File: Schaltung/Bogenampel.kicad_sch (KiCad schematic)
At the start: 36 parts, among them J1 WS2812B Stripe Timer, J10 Display, J2 Conn_01x04_Pin, J3 DC/DC Boost, J4 Jumper: 5V/Ext Voltage, J5 Buzzer, J6 Battery, J7 Input 4, J8 Input 5, J9 Power Bank, Q1 IRLZ44N, U1 NRF24L01_Breakout, U2 TXS0108EPW, U3 LM1117DT-3.3

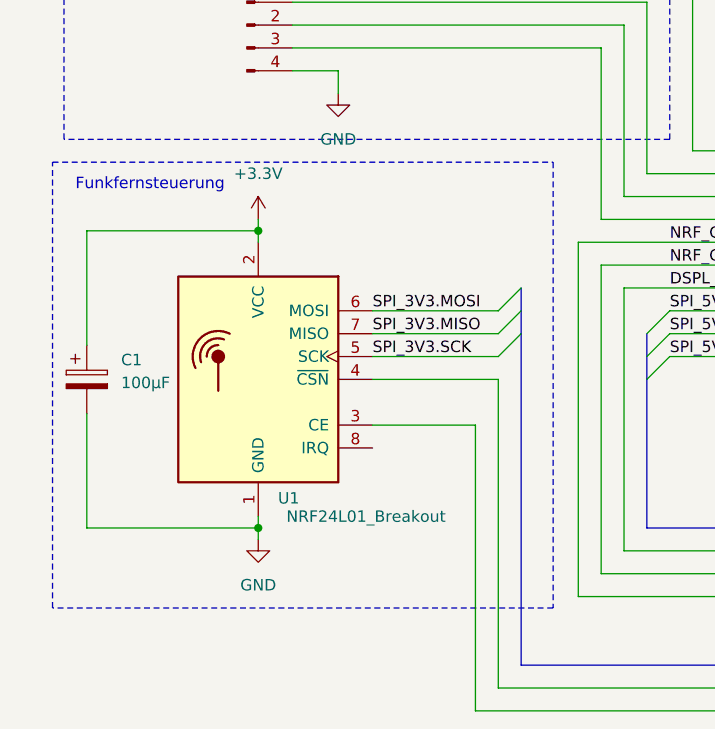
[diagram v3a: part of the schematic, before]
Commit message: DEBUG_SHORT_TIMES aktiviert mit optimierten Zeiten
Software-Änderungen:
- DEBUG_SHORT_TIMES auf 1 gesetzt (aktiviert)
- Vorbereitungsphase: 5 Sekunden (unverändert)
- Schießzeit: 15 Sekunden für beide Modi (statt 6s/12s)
- Gelbe Ampel: Aktivierung in den letzten 5 Sekunden (statt 30s)
- Empfänger Serial Baud: 115200 statt 57600
- CMD_STOP Handler vereinfacht (nur Vorbereitung zurücksetzen)

Schaltungs-Änderungen:
- MOSFET Q1 Footprint: TO-220-3_Vertical statt Horizontal
- 100nF SMD-Entkopplungskondensator (C10) hinzugefügt
- Spannungsversorgung verbessert

🤖 Generated with [Claude Code](https://claude.com/claude-code)

Co-Authored-By: Claude Sonnet 4.5 <noreply@anthropic.com>
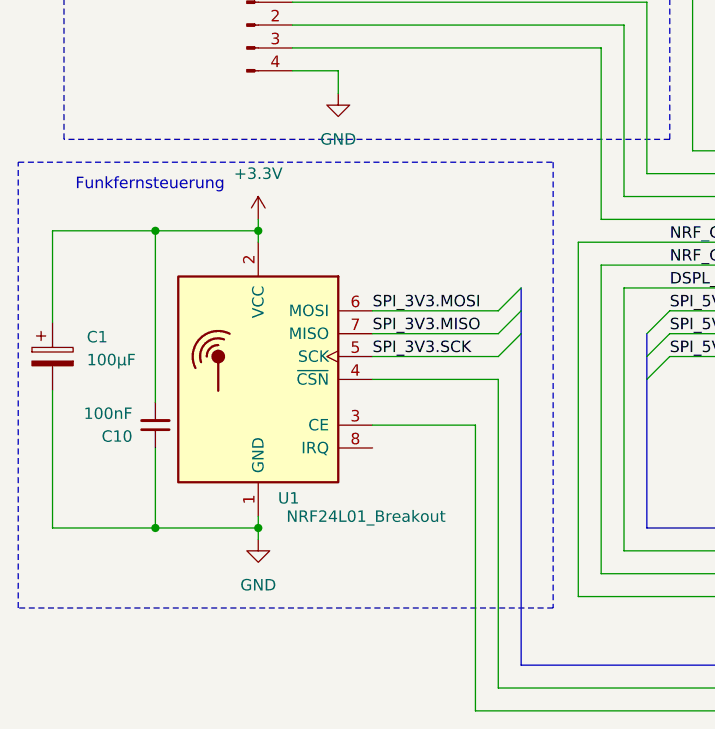
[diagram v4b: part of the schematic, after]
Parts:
- added C10: 100nF, Capacitor_SMD:C_1206_3216Metric, symbol Device:C_Small
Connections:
- net +3.3V: now also C10.2
- net GND: now also C10.1
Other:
- moved on the sheet: C1
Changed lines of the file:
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@@
 	)
 	(rectangle
-		(start 16.51 102.87)
+		(start 12.7 102.87)
 		(end 72.136 152.4)
 		(stroke
@@
 	)
 	(junction
+		(at 27.94 143.51)
+		(diameter 0)
+		(color 0 0 0 0)
+	)
+	(junction
 		(at 215.9 105.41)
 		(diameter 0)
@@
 	)
 	(junction
+		(at 27.94 110.49)
+		(diameter 0)
+		(color 0 0 0 0)
+	)
+	(junction
 		(at 39.37 143.51)
 		(diameter 0)
@@
 	(wire
 		(pts
+			(xy 27.94 110.49) (xy 16.51 110.49)
+		)
+		(stroke
+			(width 0)
+			(type default)
+		)
+	)
+	(wire
+		(pts
 			(xy 212.09 105.41) (xy 215.9 105.41)
 		)
@@
 	(wire
 		(pts
-			(xy 39.37 110.49) (xy 20.32 110.49)
+			(xy 39.37 110.49) (xy 27.94 110.49)
 		)
 		(stroke
@@
 	(wire
 		(pts
+			(xy 27.94 134.62) (xy 27.94 143.51)
+		)
+		(stroke
+			(width 0)
+			(type default)
+		)
+	)
+	(wire
+		(pts
 			(xy 63.5 163.83) (xy 63.5 132.08)
 		)
@@
 	(wire
 		(pts
+			(xy 27.94 143.51) (xy 39.37 143.51)
+		)
+		(stroke
+			(width 0)
+			(type default)
+		)
+	)
+	(wire
+		(pts
 			(xy 158.75 95.25) (xy 162.56 95.25)
 		)
@@
 	(wire
 		(pts
-			(xy 20.32 130.81) (xy 20.32 143.51)
+			(xy 16.51 128.27) (xy 16.51 143.51)
 		)
 		(stroke
@@
 	(wire
 		(pts
-			(xy 20.32 143.51) (xy 39.37 143.51)
+			(xy 16.51 143.51) (xy 27.94 143.51)
 		)
 		(stroke
@@
 	(wire
 		(pts
+			(xy 27.94 110.49) (xy 27.94 129.54)
+		)
+		(stroke
+			(width 0)
+			(type default)
+		)
+	)
+	(wire
+		(pts
 			(xy 248.92 129.54) (xy 270.51 129.54)
 		)
@@
 	(wire
 		(pts
-			(xy 20.32 110.49) (xy 20.32 123.19)
+			(xy 16.51 110.49) (xy 16.51 120.65)
 		)
 		(stroke
@@
 	(symbol
 		(lib_id "Device:C_Polarized")
-		(at 20.32 127 0)
+		(at 16.51 124.46 0)
 		(unit 1)
 		(exclude_from_sim no)
@@
 		(fields_autoplaced yes)
 		(property "Reference" "C1"
-			(at 24.13 124.8409 0)
+			(at 20.32 122.3009 0)
 			(effects
 				(font
@@
 		)
 		(property "Value" "100µF"
-			(at 24.13 127.3809 0)
+			(at 20.32 124.8409 0)
 			(effects
 				(font
@@
 		)
 		(property "Footprint" "Capacitor_THT:CP_Radial_D8.0mm_P3.50mm"
-			(at 21.2852 130.81 0)
+			(at 17.4752 128.27 0)
 			(effects
 				(font
@@
 		)
 		(property "Datasheet" "~"
-			(at 20.32 127 0)
+			(at 16.51 124.46 0)
 			(effects
 				(font
@@
 		)
 		(property "Description" "Polarized capacitor"
-			(at 20.32 127 0)
+			(at 16.51 124.46 0)
 			(effects
 				(font
@@
 					(unit 1)
 				)
+			)
+		)
+	)
+	(symbol
+		(lib_id "Device:C_Small")
+		(at 27.94 132.08 180)
+		(unit 1)
+		(exclude_from_sim no)
+		(in_bom yes)
+		(on_board yes)
+		(dnp no)
+		(property "Reference" "C10"
+			(at 25.4 133.3438 0)
+			(effects
+				(font
+					(size 1.27 1.27)
+				)
+				(justify left)
+			)
+		)
+		(property "Value" "100nF"
+			(at 25.4 130.8038 0)
+			(effects
+				(font
+					(size 1.27 1.27)
+				)
+				(justify left)
+			)
+		)
+		(property "Footprint" "Capacitor_SMD:C_1206_3216Metric"
+			(at 27.94 132.08 0)
+			(effects
+				(font
+					(size 1.27 1.27)
+				)
+				(hide yes)
+			)
+		)
+		(property "Datasheet" "~"
+			(at 27.94 132.08 0)
+			(effects
+				(font
+					(size 1.27 1.27)
+				)
+				(hide yes)
+			)
+		)
+		(property "Description" "Unpolarized capacitor, small symbol"
+			(at 27.94 132.08 0)
+			(effects
+				(font
+					(size 1.27 1.27)
+				)
+				(hide yes)
+			)
+		)
+		(pin "2"
+		)
+		(pin "1"
+		)
+		(instances
+			(project "Bogenampel"
+				(path "/4c9d4d24-7087-45e2-abcf-cdd5e2da37eb"
+					(reference "C10")
+					(unit 1)
+				)
